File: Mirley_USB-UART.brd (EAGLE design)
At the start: 52 x 69.4 mm, 34 parts, among them J1 61301611121, J2 61301611121, T1 BC817U, T2 BC817U, T3 BC817U

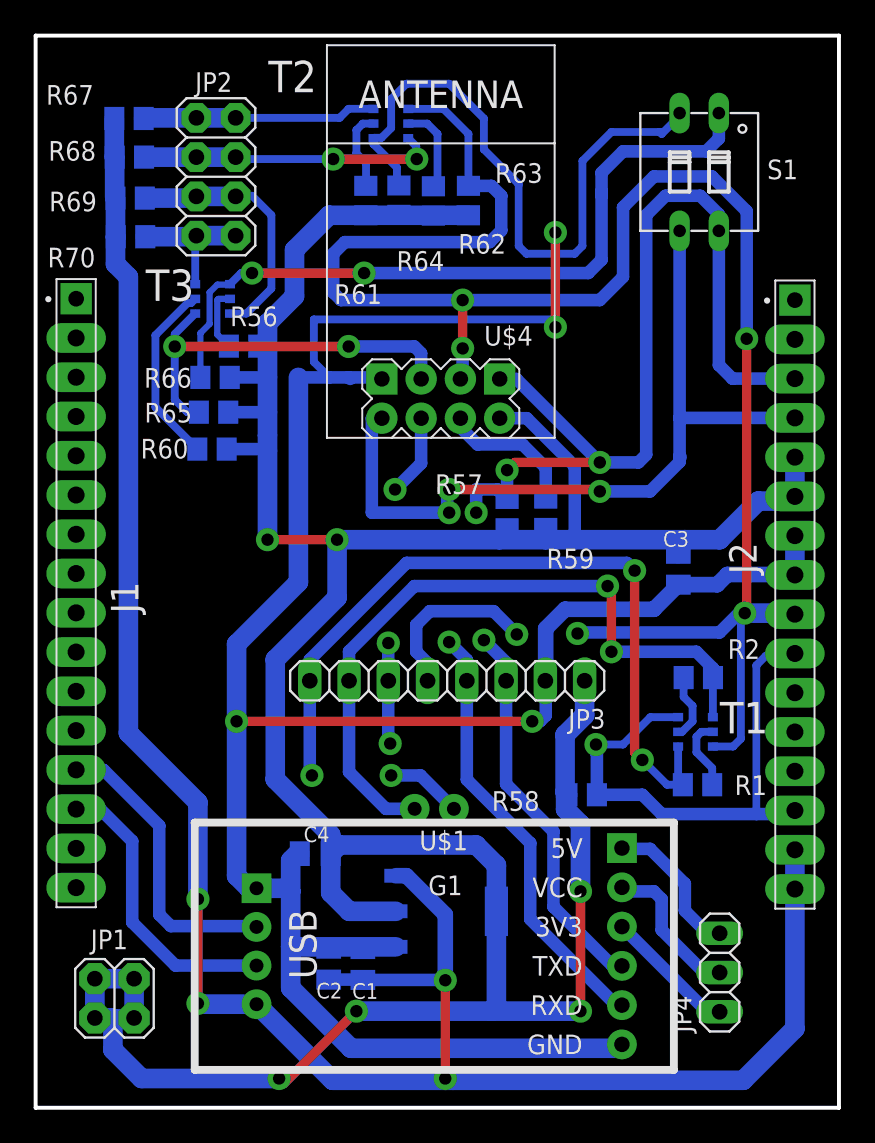
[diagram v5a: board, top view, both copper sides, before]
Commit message: zmniejszona szerokosc sciezek pod tranzystorami
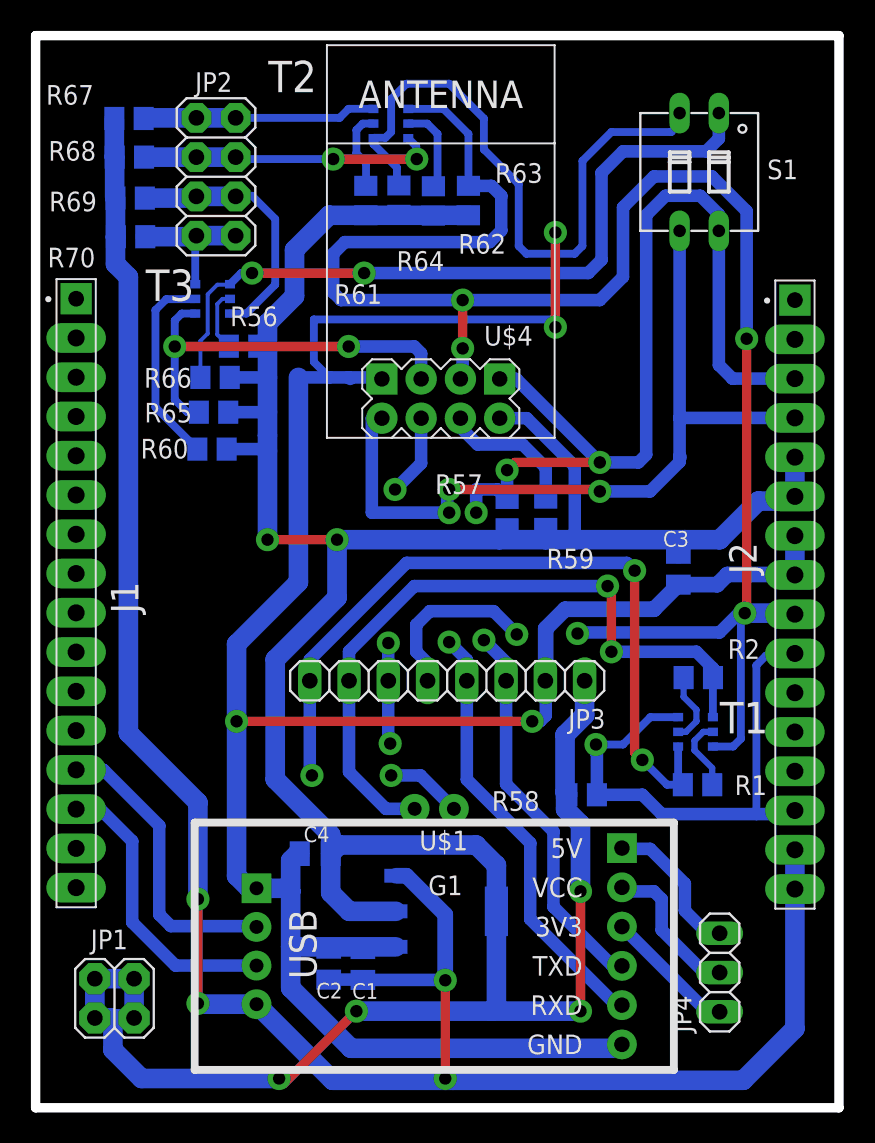
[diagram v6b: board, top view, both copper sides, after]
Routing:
- net N$19: track 12.0 -> 13.0 mm
- net GPIO2: track 25.9 -> 26.4 mm
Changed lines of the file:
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@@
 <fusionsync huburn="a.cGVyc29uYWw6dWUyYWQyNmIw" projecturn="a.cGVyc29uYWw6dWUyYWQyNmIwIzIwMTcxMDAyOTYyNDI1MjY" f3durn="urn:adsk.wipprod:dm.lineage:02zjxN1eRpiq7mc6_NkvJQ" pcbguid="da2ff9f6-32a4-4747-98e8-715e0373e83b" lastpulledtime="" lastsyncedchangeguid="21b30f2c-eae6-c85a-818a-e9b05e58b386"/>
 <plain>
-<wire x1="0" y1="0" x2="51.97" y2="0" width="0.254" layer="20"/>
-<wire x1="51.97" y1="0" x2="51.97" y2="69.36" width="0.254" layer="20"/>
-<wire x1="51.97" y1="69.36" x2="0" y2="69.36" width="0.254" layer="20"/>
-<wire x1="0" y1="69.36" x2="0" y2="0" width="0.254" layer="20"/>
+<wire x1="0" y1="0" x2="51.97" y2="0" width="0.6096" layer="20"/>
+<wire x1="51.97" y1="0" x2="51.97" y2="69.36" width="0.6096" layer="20"/>
+<wire x1="51.97" y1="69.36" x2="0" y2="69.36" width="0.6096" layer="20"/>
+<wire x1="0" y1="69.36" x2="0" y2="0" width="0.6096" layer="20"/>
 <wire x1="19" y1="68.5" x2="19" y2="43.5" width="0.8128" layer="37"/>
 <wire x1="19" y1="43.5" x2="33.5" y2="43.5" width="0.8128" layer="37"/>
@@
 <contactref element="T1" pad="5"/>
 <wire x1="41.75" y1="27.66" x2="41.92" y2="27.83" width="0.6096" layer="16"/>
-<wire x1="41.565" y1="24.32" x2="41.82" y2="24.32" width="0.508" layer="16"/>
-<wire x1="41.92" y1="26.58" x2="42.5" y2="26" width="0.508" layer="16"/>
-<wire x1="41.92" y1="26.58" x2="41.92" y2="27.83" width="0.508" layer="16"/>
-<wire x1="41.82" y1="24.32" x2="42.5" y2="25" width="0.508" layer="16"/>
-<wire x1="42.5" y1="25" x2="42.5" y2="26" width="0.508" layer="16"/>
+<wire x1="41.565" y1="24.32" x2="42.07" y2="24.32" width="0.4064" layer="16"/>
+<wire x1="41.92" y1="26.58" x2="42.75" y2="25.75" width="0.4064" layer="16"/>
+<wire x1="41.92" y1="26.58" x2="41.92" y2="27.83" width="0.4064" layer="16"/>
+<wire x1="42.07" y1="24.32" x2="42.75" y2="25" width="0.4064" layer="16"/>
+<wire x1="42.75" y1="25" x2="42.75" y2="25.75" width="0.4064" layer="16"/>
 </signal>
 <signal name="N$2">
 <contactref element="R1" pad="2"/>
 <contactref element="T1" pad="2"/>
-<wire x1="43.815" y1="24.32" x2="43.07" y2="24.32" width="0.508" layer="16"/>
-<wire x1="43.77" y1="21.98" x2="43.77" y2="20.9" width="0.508" layer="16"/>
-<wire x1="43.07" y1="24.32" x2="42.75" y2="24" width="0.508" layer="16"/>
-<wire x1="42.75" y1="24" x2="42.75" y2="23" width="0.508" layer="16"/>
-<wire x1="42.75" y1="23" x2="43.77" y2="21.98" width="0.508" layer="16"/>
+<wire x1="43.815" y1="24.32" x2="43.195" y2="24.32" width="0.4064" layer="16"/>
+<wire x1="43.77" y1="21.98" x2="43.77" y2="20.9" width="0.4064" layer="16"/>
+<wire x1="43.195" y1="24.32" x2="42.625" y2="23.75" width="0.4064" layer="16"/>
+<wire x1="42.625" y1="23.75" x2="42.625" y2="23.125" width="0.4064" layer="16"/>
+<wire x1="42.625" y1="23.125" x2="43.77" y2="21.98" width="0.4064" layer="16"/>
 </signal>
 <signal name="RESET">
@@
 <wire x1="20.25" y1="49.25" x2="9" y2="49.25" width="0.6096" layer="1"/>
 <via x="9" y="49.25" extent="1-16" drill="0.8" diameter="1.5"/>
-<wire x1="10.325" y1="51.38" x2="9" y2="50.055" width="0.508" layer="16"/>
-<wire x1="9" y1="50.055" x2="9" y2="49.25" width="0.508" layer="16"/>
+<wire x1="10.325" y1="51.38" x2="9.45" y2="51.38" width="0.508" layer="16"/>
+<wire x1="9.45" y1="51.38" x2="9" y2="50.93" width="0.508" layer="16"/>
+<wire x1="9" y1="50.93" x2="9" y2="49.25" width="0.508" layer="16"/>
 <wire x1="9" y1="49.25" x2="9" y2="45.81" width="0.508" layer="16"/>
 <wire x1="9" y1="45.81" x2="9.81" y2="45" width="0.508" layer="16"/>
@@
 <wire x1="23.375" y1="59.79" x2="23.5" y2="59.665" width="0.508" layer="16"/>
 <wire x1="21.855" y1="62.72" x2="21.885" y2="62.75" width="0.508" layer="16"/>
-<wire x1="21.885" y1="62.75" x2="22.375" y2="62.75" width="0.508" layer="16"/>
-<wire x1="22.375" y1="62.75" x2="23" y2="63.375" width="0.508" layer="16"/>
+<wire x1="21.885" y1="62.75" x2="22.625" y2="62.75" width="0.508" layer="16"/>
+<wire x1="22.625" y1="62.75" x2="23" y2="63.125" width="0.508" layer="16"/>
 <wire x1="23" y1="65.25" x2="24" y2="66.25" width="0.508" layer="16"/>
-<wire x1="23" y1="63.375" x2="23" y2="65.25" width="0.508" layer="16"/>
+<wire x1="23" y1="63.125" x2="23" y2="65.25" width="0.508" layer="16"/>
 <contactref element="S1" pad="2"/>
 <wire x1="41.75" y1="64.44" x2="41.66" y2="64.35" width="0.508" layer="16"/>
@@
 <wire x1="34.875" y1="55.25" x2="35.375" y2="55.75" width="0.508" layer="16"/>
 <wire x1="35.375" y1="61.25" x2="37.25" y2="63.125" width="0.508" layer="16"/>
-<wire x1="37.25" y1="63.125" x2="40.375" y2="63.125" width="0.508" layer="16"/>
-<wire x1="40.375" y1="63.125" x2="40.5" y2="63" width="0.508" layer="16"/>
-<wire x1="40.5" y1="63" x2="41.75" y2="64.25" width="0.508" layer="16"/>
 <wire x1="41.75" y1="64.25" x2="41.75" y2="64.44" width="0.508" layer="16"/>
 <wire x1="29" y1="62" x2="31.25" y2="59.75" width="0.508" layer="16"/>
 <wire x1="35.375" y1="55.75" x2="35.375" y2="61.25" width="0.508" layer="16"/>
+<wire x1="41.75" y1="63.75" x2="41.75" y2="64.25" width="0.508" layer="16"/>
+<wire x1="37.25" y1="63.125" x2="41.125" y2="63.125" width="0.508" layer="16"/>
+<wire x1="41.125" y1="63.125" x2="41.75" y2="63.75" width="0.508" layer="16"/>
 </signal>
 <signal name="GPIO3">
@@
 <contactref element="T3" pad="4"/>
 <wire x1="12.575" y1="53.28" x2="12.545" y2="53.25" width="0.4064" layer="16"/>
-<wire x1="11.7556" y1="53.25" x2="11.2556" y2="52.75" width="0.4064" layer="16"/>
-<wire x1="10.66" y1="50.11210625" x2="10.66" y2="47.25" width="0.4064" layer="16"/>
-<wire x1="11.2556" y1="52.75" x2="11.2556" y2="50.70770625" width="0.4064" layer="16"/>
-<wire x1="11.2556" y1="50.70770625" x2="10.66" y2="50.11210625" width="0.4064" layer="16"/>
-<wire x1="12.545" y1="53.25" x2="11.7556" y2="53.25" width="0.4064" layer="16"/>
+<wire x1="11.7556" y1="53.25" x2="11.1306" y2="52.625" width="0.254" layer="16"/>
+<wire x1="10.66" y1="49.61210625" x2="10.66" y2="47.25" width="0.254" layer="16"/>
+<wire x1="11.1306" y1="52.625" x2="11.1306" y2="50.08270625" width="0.254" layer="16"/>
+<wire x1="11.1306" y1="50.08270625" x2="10.66" y2="49.61210625" width="0.254" layer="16"/>
+<wire x1="12.545" y1="53.25" x2="11.7556" y2="53.25" width="0.254" layer="16"/>
 <wire x1="12.575" y1="53.28" x2="13.295" y2="54" width="0.508" layer="16"/>
 <wire x1="13.295" y1="54" x2="14" y2="54" width="0.508" layer="16"/>
@@
 <wire x1="14" y1="54" x2="21.25" y2="54" width="0.6096" layer="1"/>
 <via x="21.25" y="54" extent="1-16" drill="0.8" diameter="1.5"/>
-<wire x1="36.6114" y1="54.8614" x2="36.6114" y2="59" width="0.8128" layer="16"/>
-<wire x1="36.6114" y1="59" x2="36.6114" y2="59.3014" width="0.8128" layer="16"/>
+<wire x1="36.6114" y1="54.8614" x2="36.6114" y2="60.4864" width="0.8128" layer="16"/>
 <wire x1="21.25" y1="54" x2="35.75" y2="54" width="0.8128" layer="16"/>
 <wire x1="35.75" y1="54" x2="36.6114" y2="54.8614" width="0.8128" layer="16"/>
@@
 <wire x1="43.375" y1="61.875" x2="38" y2="61.875" width="0.8128" layer="16"/>
 <wire x1="38" y1="61.875" x2="36.6114" y2="60.4864" width="0.8128" layer="16"/>
-<wire x1="36.6114" y1="60.4864" x2="36.6114" y2="59.3014" width="0.8128" layer="16"/>
 <wire x1="44.2" y1="62.7" x2="43.375" y2="61.875" width="0.8128" layer="16"/>
 </signal>
@@
 <contactref element="T3" pad="2"/>
 <contactref element="R60" pad="2"/>
-<wire x1="10.325" y1="52.33" x2="10.0564" y2="52.0614" width="0.508" layer="16"/>
-<wire x1="10.0564" y1="52.0614" x2="9.8316625" y2="52.0614" width="0.508" layer="16"/>
-<wire x1="9.8316625" y1="52.0614" x2="7.75" y2="49.9797375" width="0.508" layer="16"/>
+<wire x1="10.325" y1="52.33" x2="10.3064" y2="52.3114" width="0.508" layer="16"/>
+<wire x1="10.3064" y1="52.3114" x2="8.4566625" y2="52.3114" width="0.508" layer="16"/>
+<wire x1="8.4566625" y1="52.3114" x2="7.75" y2="51.6047375" width="0.508" layer="16"/>
 <wire x1="7.75" y1="45.32" x2="10.46" y2="42.61" width="0.508" layer="16"/>
-<wire x1="7.75" y1="49.9797375" x2="7.75" y2="45.32" width="0.508" layer="16"/>
+<wire x1="7.75" y1="51.6047375" x2="7.75" y2="45.32" width="0.508" layer="16"/>
 </signal>
 <signal name="N$21">
@@
 <contactref element="T3" pad="5"/>
 <wire x1="12.575" y1="52.33" x2="12.495" y2="52.25" width="0.4064" layer="16"/>
-<wire x1="12.575" y1="52.33" x2="11.83" y2="52.33" width="0.4064" layer="16"/>
-<wire x1="11.83" y1="52.33" x2="11.75" y2="52.25" width="0.4064" layer="16"/>
-<wire x1="11.75" y1="52.25" x2="11.75" y2="50.02" width="0.4064" layer="16"/>
-<wire x1="11.75" y1="50.02" x2="12.5" y2="49.27" width="0.4064" layer="16"/>
+<wire x1="12.575" y1="52.33" x2="12.08" y2="52.33" width="0.254" layer="16"/>
+<wire x1="12.08" y1="52.33" x2="11.75" y2="52" width="0.254" layer="16"/>
+<wire x1="11.75" y1="52" x2="11.75" y2="50.02" width="0.254" layer="16"/>
+<wire x1="11.75" y1="50.02" x2="12.5" y2="49.27" width="0.254" layer="16"/>
 </signal>
 <signal name="SDA">
@@
 <wire x1="12.98" y1="59" x2="12.94" y2="58.96" width="0.8128" layer="16"/>
 <wire x1="12.575" y1="51.38" x2="13.63" y2="51.38" width="0.508" layer="16"/>
-<wire x1="15.25" y1="53" x2="15.25" y2="57.75" width="0.508" layer="16"/>
-<wire x1="13.63" y1="51.38" x2="15.25" y2="53" width="0.508" layer="16"/>
-<wire x1="15.25" y1="57.75" x2="14" y2="59" width="0.508" layer="16"/>
+<wire x1="15.5" y1="53.25" x2="15.5" y2="57.5" width="0.508" layer="16"/>
+<wire x1="13.63" y1="51.38" x2="15.5" y2="53.25" width="0.508" layer="16"/>
+<wire x1="15.5" y1="57.5" x2="14" y2="59" width="0.508" layer="16"/>
 <wire x1="14" y1="59" x2="12.98" y2="59" width="0.508" layer="16"/>
 </signal>
